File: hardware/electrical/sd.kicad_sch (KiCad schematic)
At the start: 9 parts, among them J3 Micro_SD_Card_Det2

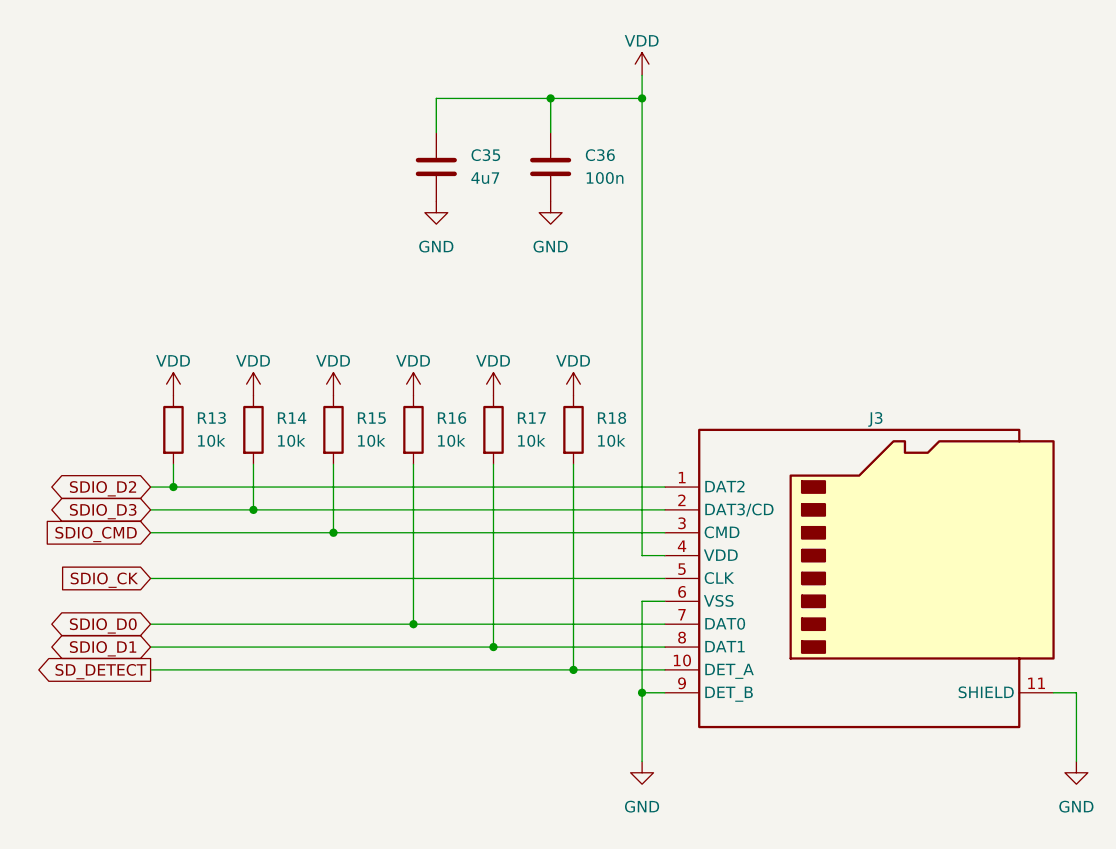
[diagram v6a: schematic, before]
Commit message: Add XKTF-N02-N footprint
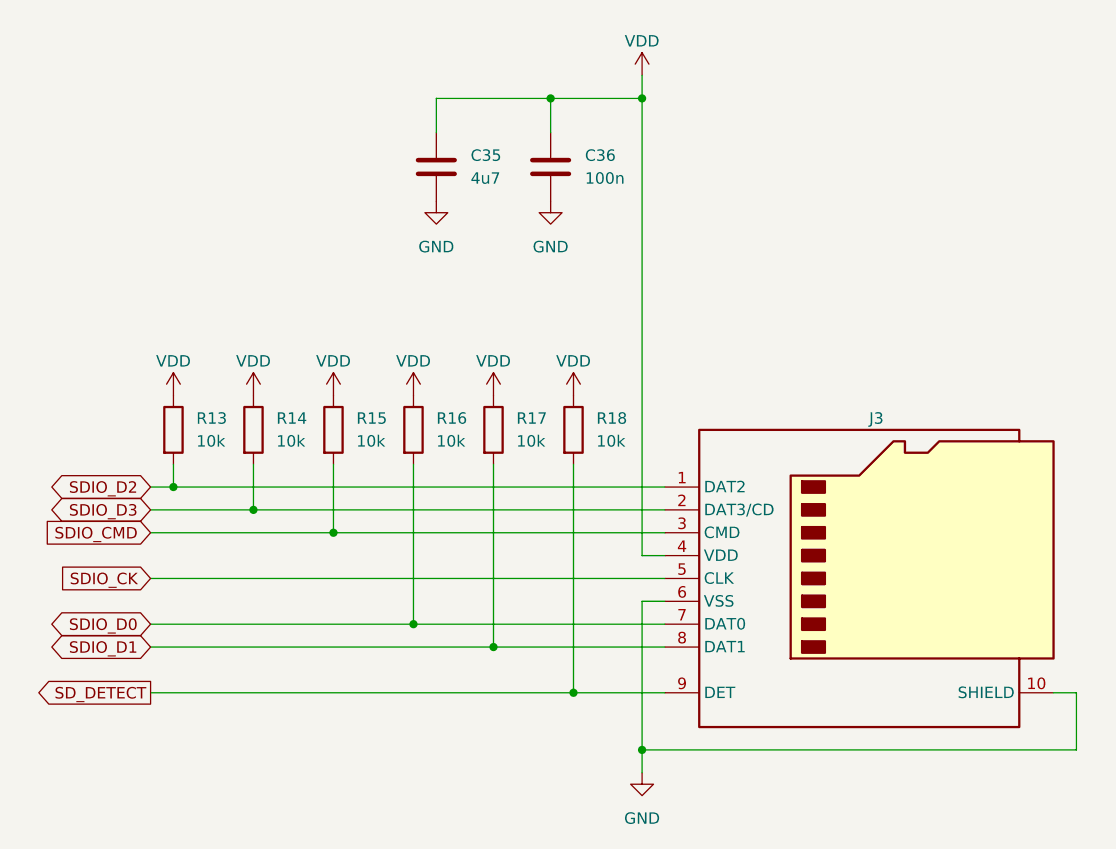
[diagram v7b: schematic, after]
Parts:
- removed J3: Micro_SD_Card_Det2, symbol Connector:Micro_SD_Card_Det2
- added J3: Micro_SD_Card_Det1, 3885:microSD_HC_XKB_XKTF-N02-N, symbol Connector:Micro_SD_Card_Det1
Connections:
- net GND: now also J3.10 (SHIELD), J3.6 (VSS)
- net SDIO_CK: now also J3.5 (CLK)
- net SDIO_CMD: now also J3.3 (CMD)
- net SDIO_D0: now also J3.7 (DAT0)
- net SDIO_D1: now also J3.8 (DAT1)
- net SDIO_D2: now also J3.1 (DAT2)
- net SDIO_D3: now also J3.2 (DAT3/CD)
- net SD_DETECT: now also J3.9 (DET)
- net VDD: now also J3.4 (VDD)
